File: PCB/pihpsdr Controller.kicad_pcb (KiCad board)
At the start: 2 copper layers, 243 x 154 mm, 168 parts, among them IC1 MCP23017T-E_SO, IC2 MCP23017T-E_SO, IC3 M24C32-RDW6TP, IC6 WM8960CGEFL_V, IC7 DS3231MZ_V+, IC8 Pico, J1 615008143721, J2 1725672, J3 485-1992, J4 SJ-3566AN, J5 SJ-3523-SMT-TR, J6 10129379-905001BLF, J7 Conn_01x02, J8 PJ-102AH, J9 MJ-3523-SMT, Q1 FDD6685, Q2 2N7002K, SW0 B3F-1055, SW1 B3F-1055, SW10 B3F-1055, SW11 B3F-1055, SW12 B3F-1055, SW13 B3F-1055, SW14 B3F-1055, SW15 B3F-1055, SW16 B3F-1055, SW17 SW_SPST, SW2 B3F-1055, SW3 B3F-1055, SW4 B3F-1055, SW5 B3F-1055, SW6 B3F-1055, SW7 B3F-1055, SW8 B3F-1055, SW9 B3F-1055, U1 LMZ22005TZ_NOPB, U2 BAT-HLD-001, Y1 TSX-3225_24.0000MF18X-C

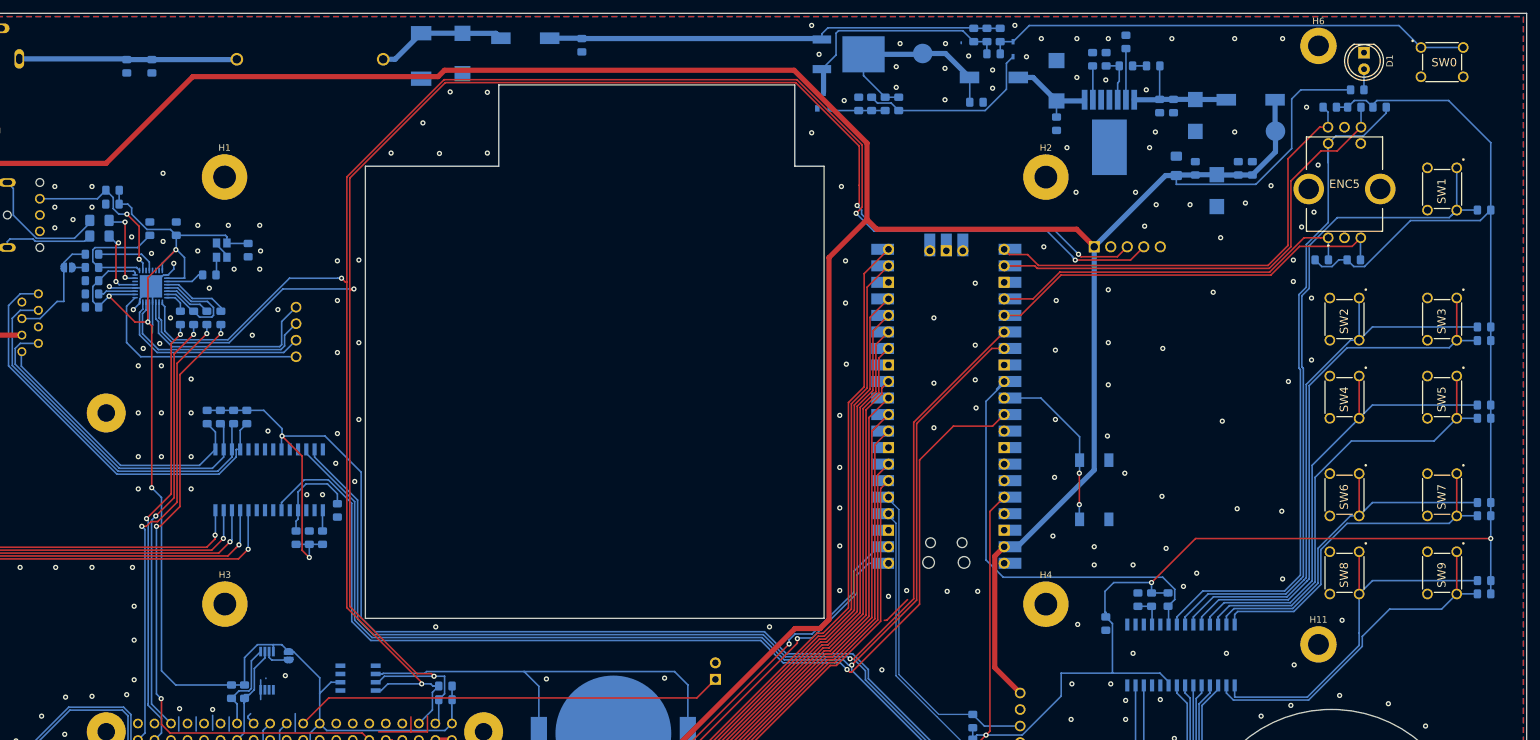
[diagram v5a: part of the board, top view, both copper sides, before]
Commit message: Replaced Side Buttons and E5. Relocated HP Capacitors.
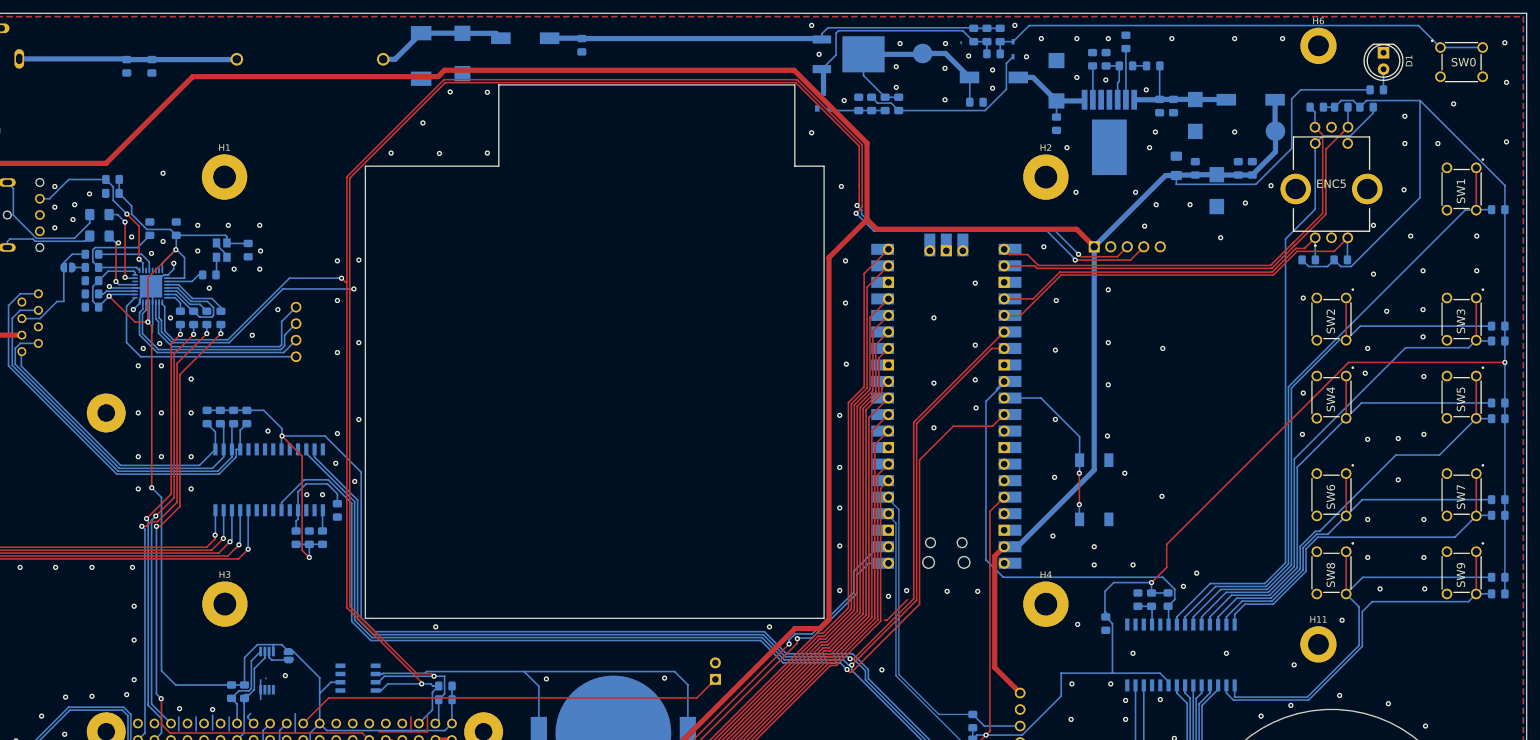
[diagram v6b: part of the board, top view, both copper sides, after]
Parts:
- moved D1 3.00 mm to (246.0, 21.0)
- moved R30 3.00 mm to (245.0, 26.8)
- moved SW0 3.00 mm to (258.0, 22.5)
- moved SW1 3.00 mm to (258.0, 42.0)
- moved SW3 3.00 mm to (258.0, 62.0)
- moved SW5 3.00 mm to (258.0, 74.0)
- moved SW7 3.00 mm to (258.0, 89.0)
- moved SW9 3.00 mm to (258.0, 101.0)
- moved R25 2.23 mm to (263.6, 101.7)
- moved R23 2.22 mm to (263.6, 89.8)
- moved R21 2.21 mm to (263.6, 74.9)
- moved R19 2.18 mm to (263.6, 63.1)
- moved R18 2.18 mm to (263.6, 45.2)
- moved R20 2.18 mm to (263.6, 65.4)
- moved R22 2.18 mm to (263.6, 77.3)
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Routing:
- net +3V3: track 738.8 -> 761.6 mm
- net SW1: track 109.1 -> 96.7 mm
- net ENC5_BTN: track 105.9 -> 99.4 mm
- net SW3: track 85.1 -> 79.7 mm
- net SW5: track 69.6 -> 64.4 mm
- net SW8: track 57.7 -> 62.9 mm
- net SW9: track 54.4 -> 58.8 mm
- net +5V: track 521.7 -> 524.7 mm
- net Net-(C17-Pad2): track 75.5 -> 78.5 mm
- net ENC5_B2: track 73.0 -> 70.9 mm
- net ENC5_B1: track 63.2 -> 61.2 mm
- net ENC5_A1: track 57.1 -> 55.1 mm
- net JACK_DETECT: track 26.1 -> 27.7 mm
- net SW6: track 56.8 -> 57.9 mm
- net SW7: track 54.8 -> 55.9 mm
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
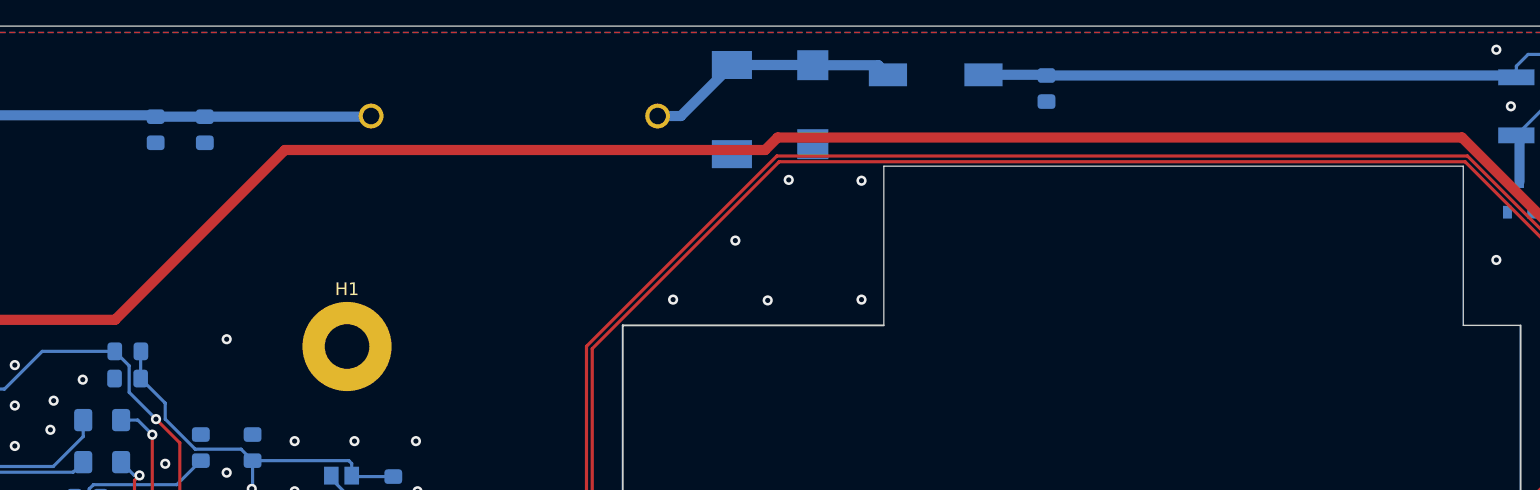
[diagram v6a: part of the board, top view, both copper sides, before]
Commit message: Made the inner breakout area for the tft smaller.
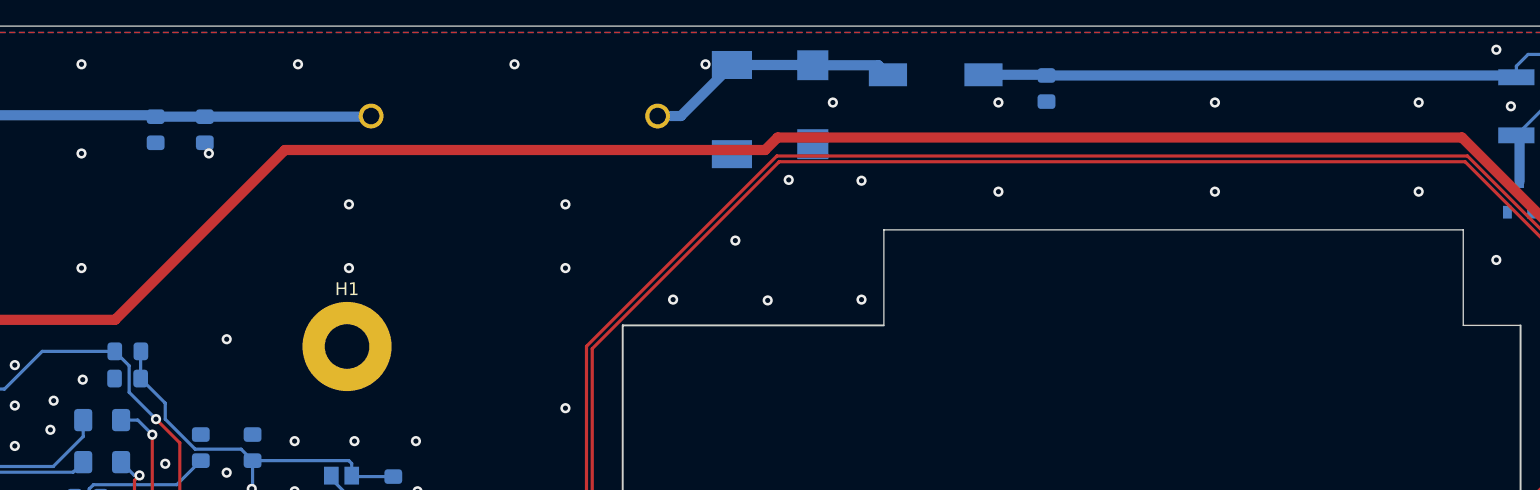
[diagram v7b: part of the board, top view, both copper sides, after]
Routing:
- net GND: vias 265 -> 284
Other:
- outline, holes or cut-outs redrawn
